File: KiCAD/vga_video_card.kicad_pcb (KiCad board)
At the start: 2 copper layers, 85 parts, among them J1 DE15_Socket_HighDensity, J2 Conn_01x20, J3 Conn_01x20, J4 Conn_01x20, J5 Conn_01x20, J6 Conn_02x16_Odd_Even, SW1 rst_btn, SW2 SW_DPDT_x2, SW3 SW_DPDT_x2, SW4 SW_DPDT_x2, U1 74HC161, U10 74HC04, U11 74HC112, U12 74HC32, U13 74HC173, U14 74HC173, U15 74HC161, U16 74HC161, U17 74HC161, U18 74HC04, U19 74HC04, U2 74HC161, U20 74HC133, U21 74HC133, U22 74HC133, U23 74HC133, U24 74HC112, U25 74HC173, U26 74HC173, U27 74HC04, U28 74HC253, U29 74HC253, U3 74HC161, U30 CY7C199, U31 CY7C199, U32 74AHC595, U33 74AHC595, U34 74AHC595, U35 AD7523JN, U36 LM358, U37 74HC257, U38 74HC257, U39 74HC02, U4 74HC04, U44 74HC257, U45 74HC257, U46 74HC257, U47 74HC257, U48 74HC257, U49 74HC257, U5 74HC04, U50 74HC257, U51 74HC257, U52 74HC4053, U53 74HC4053, U54 74HC4053, U55 74HC257, U56 74HC257, U6 74HC30, U7 74HC30, U8 74HC30, U9 74HC30, Y1 10MHz

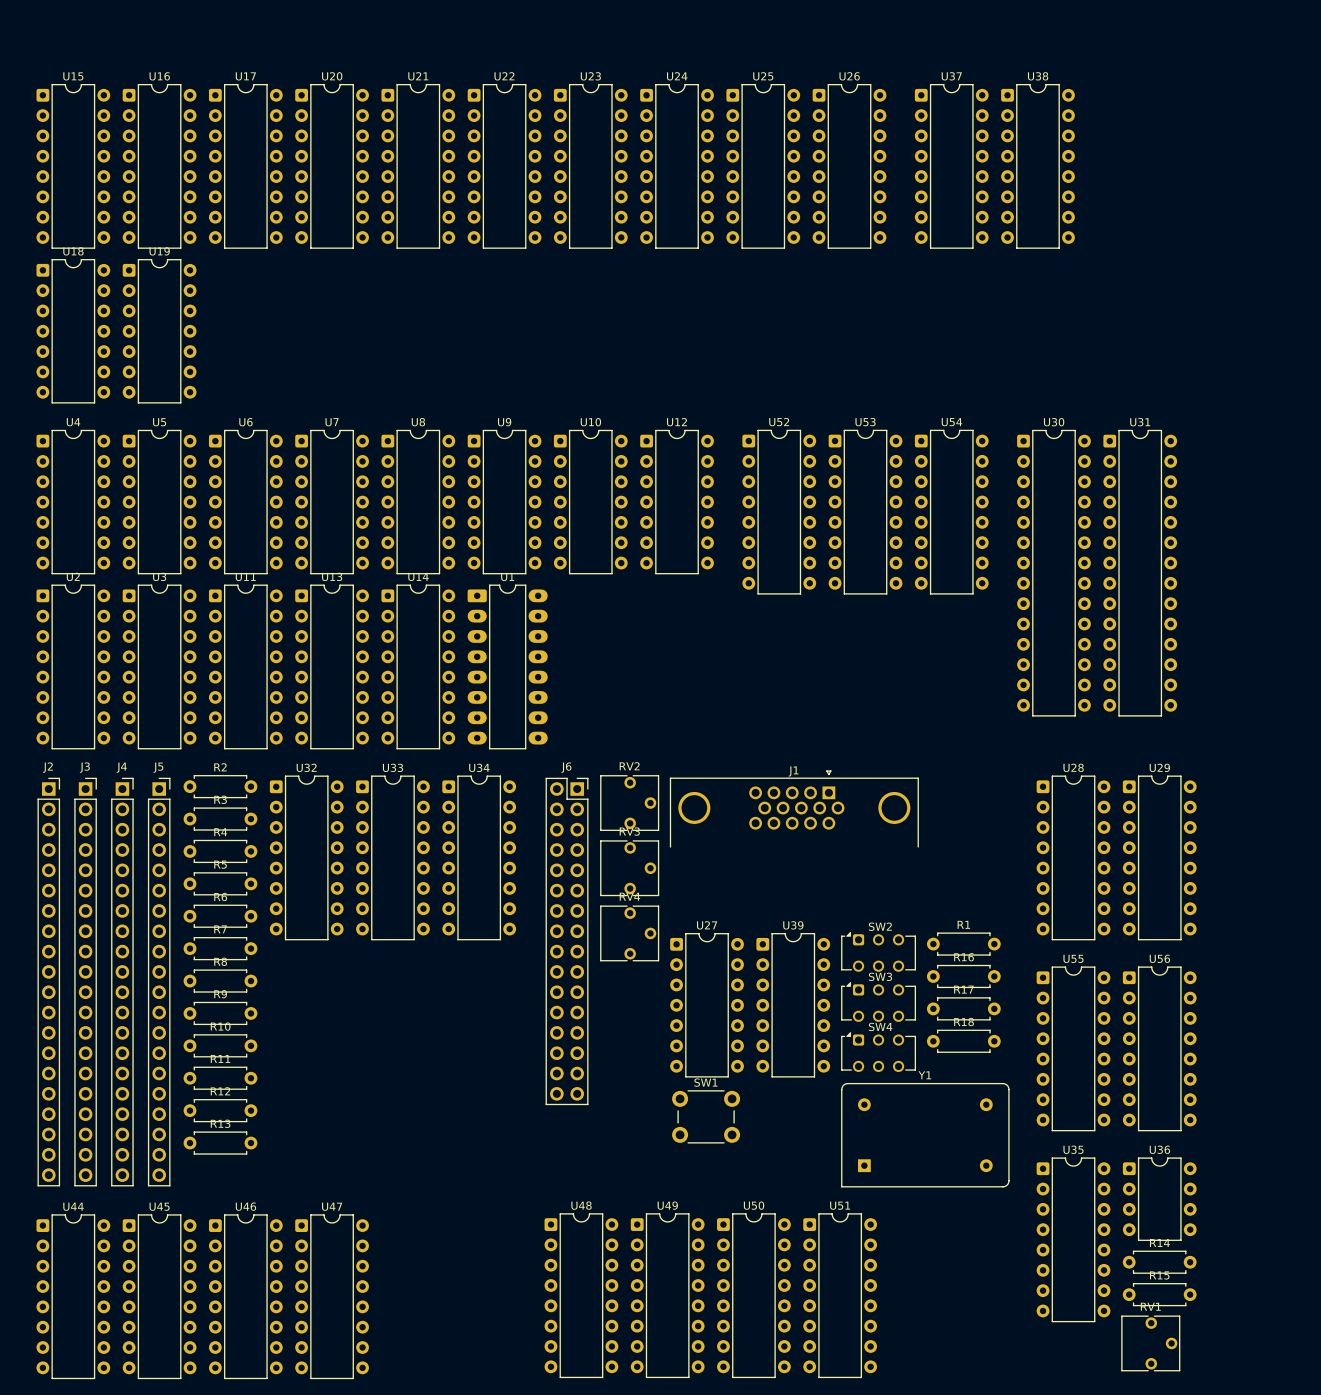
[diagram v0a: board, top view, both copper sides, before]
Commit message: modified debug connector; changed board type in pcb editor
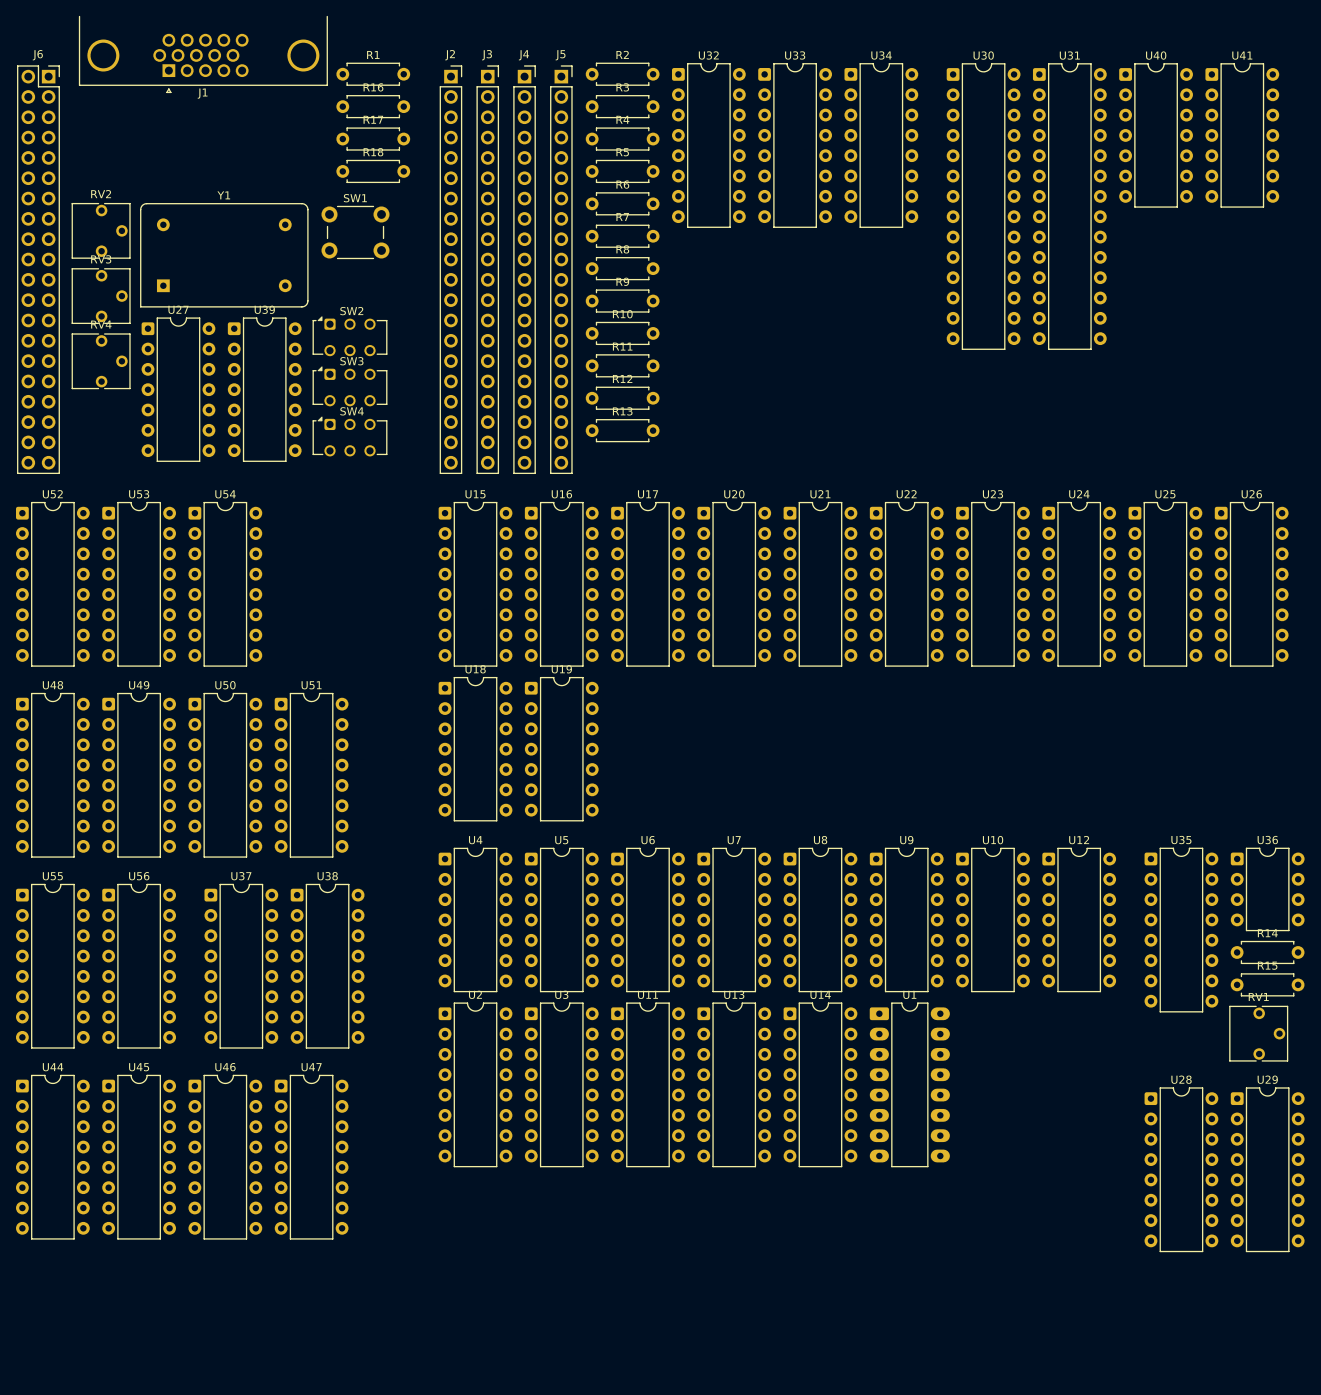
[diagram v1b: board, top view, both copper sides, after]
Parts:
- added U40: 74HC74, Package_DIP:DIP-14_W7.62mm, F.Cu at (164.4, 20.0)
- added U41: 74HC00, Package_DIP:DIP-14_W7.62mm, F.Cu at (175.2, 20.0)
- J6: value Conn_02x16_Odd_Even -> Conn_02x20_Odd_Even; footprint Connector_PinSocket_2.54mm:PinSocket_2x16_P2.54mm_Vertical -> Connector_PinSocket_2.54mm:PinSocket_2x20_P2.54mm_Vertical
- moved Y1 140.6 mm to (44.1, 46.4)
- moved U37 133.7 mm to (50.1, 122.6)
- moved U38 133.7 mm to (60.9, 122.6)
- moved R1 131.4 mm to (66.6, 19.9)
- moved R17 131.4 mm to (66.6, 28.1)
- moved R18 131.4 mm to (66.6, 32.1)
- moved R16 131.4 mm to (66.6, 24.0)
- moved U55 128.0 mm to (26.5, 122.6)
- moved U56 128.0 mm to (37.3, 122.6)
- moved J1 122.3 mm to (44.8, 19.5), turned to 180 degrees
- moved SW1 118.9 mm to (64.9, 37.5)
- moved J6 110.9 mm to (29.8, 20.2)
- moved R10 102.3 mm to (97.8, 52.4)
- moved R13 102.3 mm to (97.8, 64.5)
- moved R5 102.3 mm to (97.8, 32.1)
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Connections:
- net /RAM_module/RAM_state_controller/RAM0_~{WE} renamed /RAM0_~{WE}
- net /RAM_module/ext_graphics_source/data_rclk renamed /RAM_module/ext_graphics_rclk
- net Net-(J3-Pin_1) renamed /RAM_module/await_upd
- R1 pad 2: /horizontal_counter/manual_rst -> /mrst
- SW1 pad 1: /horizontal_counter/manual_rst -> /mrst
- U12 pad 13: /horizontal_counter/manual_rst -> /mrst
- U12 pad 5: /horizontal_counter/manual_rst -> /mrst
- U27 pad 3: unconnected-(U27-Pad3) -> (no net)
- U27 pad 4: unconnected-(U27-Pad4) -> (no net)
- U28 pad 7: /RAM_module/RAM_state_controller/RAM0_~{CE} -> /RAM0_~{CE}
- U29 pad 7: /RAM_module/RAM_state_controller/RAM1_~{CE} -> /RAM1_~{CE}
- U29 pad 9: /RAM_module/RAM_state_controller/RAM1_~{WE} -> /RAM1_~{WE}
- U30 pad 20: /RAM_module/RAM_state_controller/RAM0_~{CE} -> /RAM0_~{CE}
- U30 pad 22: /RAM_module/RAM_state_controller/RAM0_~{CE} -> /RAM0_~{CE}
- U31 pad 20: /RAM_module/RAM_state_controller/RAM1_~{CE} -> /RAM1_~{CE}
- U31 pad 22: /RAM_module/RAM_state_controller/RAM1_~{CE} -> /RAM1_~{CE}
- U31 pad 27: /RAM_module/RAM_state_controller/RAM1_~{WE} -> /RAM1_~{WE}
- U39 pad 4: unconnected-(U39-Pad4) -> /writing_RAM
- U39 pad 5: unconnected-(U39-Pad5) -> Net-(U39-Pad5)
- U39 pad 6: unconnected-(U39-Pad6) -> /mrst
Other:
- copper layers 2 -> 4

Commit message: update pcb
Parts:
- U1: footprint Package_DIP:DIP-16_W7.62mm_LongPads -> Package_DIP:DIP-16_W7.62mm
- moved U14 179.3 mm to (301.8, 134.4)
- moved J1 176.5 mm to (221.4, 18.2), turned to 0 degrees
- moved J2 168.5 mm to (248.6, 17.2)
- moved J3 168.5 mm to (253.2, 17.2)
- moved R10 168.5 mm to (266.2, 49.3)
- moved R11 168.5 mm to (266.2, 53.4)
- moved R12 168.5 mm to (266.2, 57.4)
- moved R13 168.5 mm to (266.2, 61.5)
- moved R14 168.5 mm to (346.9, 126.7)
- moved R15 168.5 mm to (346.9, 130.8)
- moved R16 168.5 mm to (235.1, 21.0)
- moved R17 168.5 mm to (235.1, 25.0)
- moved R18 168.5 mm to (235.1, 29.1)
- moved R2 168.5 mm to (266.2, 16.9)
- moved R3 168.5 mm to (266.2, 21.0)
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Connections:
- U27 pad 3: (no net) -> unconnected-(U27-Pad3)
- U27 pad 4: (no net) -> unconnected-(U27-Pad4)
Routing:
- net /horizontal_counter/CLK: track 0.00 -> 172.6 mm
- net /horizontal_counter/bit_2: track 0.00 -> 157.4 mm
- net /horizontal_counter/~{CLK}: track 0.00 -> 149.8 mm
- net /horizontal_counter/bit_0: track 0.00 -> 145.7 mm
- net /horizontal_counter/bit_3: track 0.00 -> 98.0 mm
- net /horizontal_counter/~{rst}: track 0.00 -> 67.9 mm
- net /horizontal_counter/bit_1: track 0.00 -> 60.6 mm
- net /horizontal_counter/~{bit_1}: track 0.00 -> 52.4 mm
- net /horizontal_counter/bit_7: track 0.00 -> 49.9 mm
- net /horizontal_counter/~{bit_2}: track 0.00 -> 39.9 mm
- net /horizontal_counter/bit_6: track 0.00 -> 38.9 mm
- net /horizontal_counter/bit_4: track 0.00 -> 36.0 mm
- net /horizontal_counter/bit_5: track 0.00 -> 35.1 mm
- net /horizontal_counter/~{bit_0}: track 0.00 -> 34.7 mm
- net /horizontal_counter/bit_8: track 0.00 -> 16.0 mm
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- added copper zone on In2.Cu, net +5V
- added copper zone on In1.Cu, net GND

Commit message: fix multiple ERCs that made RAM addrs not connecting
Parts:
- moved U25 285.9 mm to (48.3, 64.8)
- moved U26 282.7 mm to (62.2, 64.8)
- moved U14 270.8 mm to (34.3, 176.5)
- moved U24 261.6 mm to (62.2, 87.6)
- moved U22 256.1 mm to (48.3, 108.0)
- moved U23 253.3 mm to (62.2, 110.5)
- moved U20 239.3 mm to (48.3, 130.8)
- moved U21 236.9 mm to (62.2, 133.3)
- moved U17 235.8 mm to (48.3, 153.7)
- moved U31 228.3 mm to (116.8, 116.8)
- moved U15 225.4 mm to (48.3, 176.5)
- moved U16 222.6 mm to (62.2, 176.5)
- moved U19 210.5 mm to (48.3, 87.6)
- moved U13 205.5 mm to (20.3, 172.7)
- moved U30 199.8 mm to (111.8, 26.7)
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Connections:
- U52 pad 1: /RAM_module/RAM_bus_mux/RAM0_data1 -> /RAM_module/RAM0_d1
- U52 pad 12: /RAM_module/RAM_bus_mux/RAM1_data0 -> /RAM_module/RAM1_d0
- U52 pad 13: /RAM_module/RAM_bus_mux/RAM0_data0 -> /RAM_module/RAM0_d0
- U52 pad 2: /RAM_module/RAM_bus_mux/RAM1_data1 -> /RAM_module/RAM1_d1
- U52 pad 3: /RAM_module/RAM_bus_mux/RAM0_data2 -> /RAM_module/RAM0_d2
- U52 pad 5: /RAM_module/RAM_bus_mux/RAM1_data2 -> /RAM_module/RAM1_d2
- U53 pad 1: /RAM_module/RAM_bus_mux/RAM0_data4 -> /RAM_module/RAM0_d4
- U53 pad 12: /RAM_module/RAM_bus_mux/RAM1_data3 -> /RAM_module/RAM1_d3
- U53 pad 13: /RAM_module/RAM_bus_mux/RAM0_data3 -> /RAM_module/RAM0_d3
- U53 pad 2: /RAM_module/RAM_bus_mux/RAM1_data4 -> /RAM_module/RAM1_d4
- U53 pad 3: /RAM_module/RAM_bus_mux/RAM0_data5 -> /RAM_module/RAM0_d5
- U53 pad 5: /RAM_module/RAM_bus_mux/RAM1_data5 -> /RAM_module/RAM1_d5
- U54 pad 1: /RAM_module/RAM_bus_mux/RAM0_data7 -> /RAM_module/RAM0_d7
- U54 pad 12: /RAM_module/RAM_bus_mux/RAM1_data6 -> /RAM_module/RAM1_d6
- U54 pad 13: /RAM_module/RAM_bus_mux/RAM0_data6 -> /RAM_module/RAM0_d6
- U54 pad 2: /RAM_module/RAM_bus_mux/RAM1_data7 -> /RAM_module/RAM1_d7
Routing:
- net /horizontal_counter/CLK: track 172.6 -> 0.00 mm
- net /horizontal_counter/bit_2: track 157.4 -> 0.00 mm
- net /horizontal_counter/~{CLK}: track 149.8 -> 0.00 mm
- net /horizontal_counter/bit_0: track 145.7 -> 0.00 mm
- net /horizontal_counter/bit_3: track 98.0 -> 0.00 mm
- net /horizontal_counter/~{rst}: track 67.9 -> 0.00 mm
- net /horizontal_counter/bit_1: track 60.6 -> 0.00 mm
- net /horizontal_counter/~{bit_1}: track 52.4 -> 0.00 mm
- net /horizontal_counter/bit_7: track 49.9 -> 0.00 mm
- net /horizontal_counter/~{bit_2}: track 39.9 -> 0.00 mm
- net /horizontal_counter/bit_6: track 38.9 -> 0.00 mm
- net /horizontal_counter/bit_4: track 36.0 -> 0.00 mm
- net /horizontal_counter/bit_5: track 35.1 -> 0.00 mm
- net /horizontal_counter/~{bit_0}: track 34.7 -> 0.00 mm
- net /horizontal_counter/bit_8: track 16.0 -> 0.00 mm
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- removed copper zone on In2.Cu, net +5V
- removed copper zone on In1.Cu, net GND

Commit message: resolved all ERC errors, kicad got some stupid bugs
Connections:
- net /i_addr0 renamed /RAM_module/RAM_bus_mux/i_addr0
- net /i_addr1 renamed /RAM_module/RAM_bus_mux/i_addr1
- net /i_addr2 renamed /RAM_module/RAM_bus_mux/i_addr2
- net /i_addr3 renamed /RAM_module/RAM_bus_mux/i_addr3
- net /i_addr4 renamed /RAM_module/RAM_bus_mux/i_addr4
- net /i_addr5 renamed /RAM_module/RAM_bus_mux/i_addr5
- net /i_addr6 renamed /RAM_module/RAM_bus_mux/i_addr6
- net /i_addr7 renamed /RAM_module/RAM_bus_mux/i_addr7
- J6 pad 10: /j_addr_3 -> /RAM_module/RAM_bus_mux/j_addr3
- J6 pad 12: /j_addr_4 -> /RAM_module/RAM_bus_mux/j_addr4
- J6 pad 14: /j_addr_5 -> /RAM_module/RAM_bus_mux/j_addr5
- J6 pad 16: /j_addr_6 -> /RAM_module/RAM_bus_mux/j_addr6
- J6 pad 18: /j_addr_7 -> /RAM_module/RAM_bus_mux/j_addr7
- J6 pad 35: unconnected-(J6-Pin_35-Pad35) -> /RAM0_~{WE}
- J6 pad 4: /j_addr_0 -> /RAM_module/RAM_bus_mux/j_addr0
- J6 pad 6: /j_addr_1 -> /RAM_module/RAM_bus_mux/j_addr1
- J6 pad 8: /j_addr_2 -> /RAM_module/RAM_bus_mux/j_addr2
- U13 pad 3: /j_addr0 -> /RAM_module/RAM_bus_mux/j_addr0
- U13 pad 4: /j_addr1 -> /RAM_module/RAM_bus_mux/j_addr1
- U13 pad 5: /j_addr2 -> /RAM_module/RAM_bus_mux/j_addr2
- U13 pad 6: /j_addr3 -> /RAM_module/RAM_bus_mux/j_addr3
- U14 pad 3: /j_addr4 -> /RAM_module/RAM_bus_mux/j_addr4
- U14 pad 4: /j_addr5 -> /RAM_module/RAM_bus_mux/j_addr5
- U14 pad 5: /j_addr6 -> /RAM_module/RAM_bus_mux/j_addr6
- U14 pad 6: /j_addr7 -> /RAM_module/RAM_bus_mux/j_addr7
- U15 pad 1: unconnected-(U15-~{MR}-Pad1) -> /vertical_counter/~{rst}
- U16 pad 1: unconnected-(U16-~{MR}-Pad1) -> /vertical_counter/~{rst}
- U17 pad 1: unconnected-(U17-~{MR}-Pad1) -> /vertical_counter/~{rst}
- U25 pad 16: unconnected-(U25-VCC-Pad16) -> +5V
- U28 pad 14: /RAM_module/RAM_bus_mux/rbit_0 -> /RAM_module/RAM_bus_mux/j_addr0
- U29 pad 14: /RAM_module/RAM_bus_mux/rbit_0 -> /RAM_module/RAM_bus_mux/j_addr0
- U32 pad 1: /RAM_module/RAM_bus_mux/15bit_2:1_MUX/I1_8 -> /RAM_module/RAM_bus_mux/w_addr8
- U32 pad 2: /RAM_module/RAM_bus_mux/15bit_2:1_MUX/I1_9 -> /RAM_module/RAM_bus_mux/w_addr9
- U32 pad 3: /RAM_module/RAM_bus_mux/15bit_2:1_MUX/I1_10 -> /RAM_module/RAM_bus_mux/w_addr10
- U32 pad 4: /RAM_module/RAM_bus_mux/15bit_2:1_MUX/I1_11 -> /RAM_module/RAM_bus_mux/w_addr11
- U32 pad 5: /RAM_module/RAM_bus_mux/15bit_2:1_MUX/I1_12 -> /RAM_module/RAM_bus_mux/w_addr12
- U32 pad 6: /RAM_module/RAM_bus_mux/15bit_2:1_MUX/I1_13 -> /RAM_module/RAM_bus_mux/w_addr13
- U32 pad 7: /RAM_module/RAM_bus_mux/15bit_2:1_MUX/I1_14 -> /RAM_module/RAM_bus_mux/w_addr14
- U33 pad 1: /RAM_module/RAM_bus_mux/15bit_2:1_MUX/I1_1 -> /RAM_module/RAM_bus_mux/w_addr1
- U33 pad 15: /RAM_module/RAM_bus_mux/15bit_2:1_MUX/I1_0 -> /RAM_module/RAM_bus_mux/w_addr0
- U33 pad 2: /RAM_module/RAM_bus_mux/15bit_2:1_MUX/I1_2 -> /RAM_module/RAM_bus_mux/w_addr2
- U33 pad 3: /RAM_module/RAM_bus_mux/15bit_2:1_MUX/I1_3 -> /RAM_module/RAM_bus_mux/w_addr3
- U33 pad 4: /RAM_module/RAM_bus_mux/15bit_2:1_MUX/I1_4 -> /RAM_module/RAM_bus_mux/w_addr4
- U33 pad 5: /RAM_module/RAM_bus_mux/15bit_2:1_MUX/I1_5 -> /RAM_module/RAM_bus_mux/w_addr5
- U33 pad 6: /RAM_module/RAM_bus_mux/15bit_2:1_MUX/I1_6 -> /RAM_module/RAM_bus_mux/w_addr6
- U33 pad 7: /RAM_module/RAM_bus_mux/15bit_2:1_MUX/I1_7 -> /RAM_module/RAM_bus_mux/w_addr7
- U37 pad 10: unconnected-(U37-I1d-Pad10) -> /ADC_module/I3
- U37 pad 11: unconnected-(U37-I0d-Pad11) -> GND
- U37 pad 12: unconnected-(U37-Zc-Pad12) -> /ADC_module/D2
- U37 pad 13: unconnected-(U37-I1c-Pad13) -> /ADC_module/I2
- U37 pad 14: unconnected-(U37-I0c-Pad14) -> GND
- U37 pad 2: unconnected-(U37-I0a-Pad2) -> GND
- U37 pad 3: unconnected-(U37-I1a-Pad3) -> /ADC_module/I0
- U37 pad 4: unconnected-(U37-Za-Pad4) -> /ADC_module/D0
- U37 pad 5: unconnected-(U37-I0b-Pad5) -> GND
- U37 pad 6: unconnected-(U37-I1b-Pad6) -> /ADC_module/I1
- U37 pad 7: unconnected-(U37-Zb-Pad7) -> /ADC_module/D1
- U37 pad 9: unconnected-(U37-Zd-Pad9) -> /ADC_module/D3
- U38 pad 10: unconnected-(U38-I1d-Pad10) -> /ADC_module/I7
- U38 pad 11: unconnected-(U38-I0d-Pad11) -> GND
- U38 pad 12: unconnected-(U38-Zc-Pad12) -> /ADC_module/D6
- U38 pad 13: unconnected-(U38-I1c-Pad13) -> /ADC_module/I6
- U38 pad 14: unconnected-(U38-I0c-Pad14) -> GND
- U38 pad 2: unconnected-(U38-I0a-Pad2) -> GND
- U38 pad 3: unconnected-(U38-I1a-Pad3) -> /ADC_module/I4
- U38 pad 4: unconnected-(U38-Za-Pad4) -> /ADC_module/D4
- U38 pad 5: unconnected-(U38-I0b-Pad5) -> GND
- U38 pad 6: unconnected-(U38-I1b-Pad6) -> /ADC_module/I5
- U38 pad 7: unconnected-(U38-Zb-Pad7) -> /ADC_module/D5
- U38 pad 9: unconnected-(U38-Zd-Pad9) -> /ADC_module/D7
- U40 pad 4: unconnected-(U40A-~{S}-Pad4) -> +5V
- U44 pad 1: /RAM_module/RAM_bus_mux/rbit_0 -> /RAM_module/RAM_bus_mux/j_addr0
- U44 pad 10: unconnected-(U44-I1d-Pad10) -> /RAM_module/RAM_bus_mux/w_addr3
- U44 pad 11: unconnected-(U44-I0d-Pad11) -> /RAM_module/RAM_bus_mux/addr3
- U44 pad 12: unconnected-(U44-Zc-Pad12) -> /RAM_module/RAM0_a2
- U44 pad 13: unconnected-(U44-I1c-Pad13) -> /RAM_module/RAM_bus_mux/w_addr2
- U44 pad 14: unconnected-(U44-I0c-Pad14) -> /RAM_module/RAM_bus_mux/addr2
- U44 pad 2: unconnected-(U44-I0a-Pad2) -> /RAM_module/RAM_bus_mux/addr0
- U44 pad 3: unconnected-(U44-I1a-Pad3) -> /RAM_module/RAM_bus_mux/w_addr0
- U44 pad 4: unconnected-(U44-Za-Pad4) -> /RAM_module/RAM0_a0
- U44 pad 5: unconnected-(U44-I0b-Pad5) -> /RAM_module/RAM_bus_mux/addr1
- U44 pad 6: unconnected-(U44-I1b-Pad6) -> /RAM_module/RAM_bus_mux/w_addr1
- U44 pad 7: unconnected-(U44-Zb-Pad7) -> /RAM_module/RAM0_a1
- U44 pad 9: unconnected-(U44-Zd-Pad9) -> /RAM_module/RAM0_a3
- U45 pad 1: /RAM_module/RAM_bus_mux/rbit_0 -> /RAM_module/RAM_bus_mux/j_addr0
- U45 pad 10: unconnected-(U45-I1d-Pad10) -> /RAM_module/RAM_bus_mux/w_addr7
- U45 pad 11: unconnected-(U45-I0d-Pad11) -> /RAM_module/RAM_bus_mux/addr7
- U45 pad 12: unconnected-(U45-Zc-Pad12) -> /RAM_module/RAM0_a6
- U45 pad 13: unconnected-(U45-I1c-Pad13) -> /RAM_module/RAM_bus_mux/w_addr6
- U45 pad 14: unconnected-(U45-I0c-Pad14) -> /RAM_module/RAM_bus_mux/addr6
- U45 pad 2: unconnected-(U45-I0a-Pad2) -> /RAM_module/RAM_bus_mux/addr4
- U45 pad 3: unconnected-(U45-I1a-Pad3) -> /RAM_module/RAM_bus_mux/w_addr4
- U45 pad 4: unconnected-(U45-Za-Pad4) -> /RAM_module/RAM0_a4
- U45 pad 5: unconnected-(U45-I0b-Pad5) -> /RAM_module/RAM_bus_mux/addr5
- U45 pad 6: unconnected-(U45-I1b-Pad6) -> /RAM_module/RAM_bus_mux/w_addr5
- U45 pad 7: unconnected-(U45-Zb-Pad7) -> /RAM_module/RAM0_a5
- U45 pad 9: unconnected-(U45-Zd-Pad9) -> /RAM_module/RAM0_a7
- U46 pad 1: /RAM_module/RAM_bus_mux/rbit_0 -> /RAM_module/RAM_bus_mux/j_addr0
- U46 pad 10: unconnected-(U46-I1d-Pad10) -> /RAM_module/RAM_bus_mux/w_addr11
- U46 pad 11: unconnected-(U46-I0d-Pad11) -> /RAM_module/RAM_bus_mux/addr11
- U46 pad 12: unconnected-(U46-Zc-Pad12) -> /RAM_module/RAM0_a10
- U46 pad 13: unconnected-(U46-I1c-Pad13) -> /RAM_module/RAM_bus_mux/w_addr10
- U46 pad 14: unconnected-(U46-I0c-Pad14) -> /RAM_module/RAM_bus_mux/addr10
- U46 pad 2: unconnected-(U46-I0a-Pad2) -> /RAM_module/RAM_bus_mux/addr8
- U46 pad 3: unconnected-(U46-I1a-Pad3) -> /RAM_module/RAM_bus_mux/w_addr8
- U46 pad 4: unconnected-(U46-Za-Pad4) -> /RAM_module/RAM0_a8
- U46 pad 5: unconnected-(U46-I0b-Pad5) -> /RAM_module/RAM_bus_mux/addr9
- U46 pad 6: unconnected-(U46-I1b-Pad6) -> /RAM_module/RAM_bus_mux/w_addr9
- U46 pad 7: unconnected-(U46-Zb-Pad7) -> /RAM_module/RAM0_a9
- U46 pad 9: unconnected-(U46-Zd-Pad9) -> /RAM_module/RAM0_a11
- U47 pad 1: /RAM_module/RAM_bus_mux/rbit_0 -> /RAM_module/RAM_bus_mux/j_addr0
- U47 pad 12: unconnected-(U47-Zc-Pad12) -> /RAM_module/RAM0_a14
- U47 pad 13: unconnected-(U47-I1c-Pad13) -> /RAM_module/RAM_bus_mux/w_addr14
- U47 pad 14: unconnected-(U47-I0c-Pad14) -> /RAM_module/RAM_bus_mux/addr14
- U47 pad 2: unconnected-(U47-I0a-Pad2) -> /RAM_module/RAM_bus_mux/addr12
- U47 pad 3: unconnected-(U47-I1a-Pad3) -> /RAM_module/RAM_bus_mux/w_addr12
- U47 pad 4: unconnected-(U47-Za-Pad4) -> /RAM_module/RAM0_a12
- U47 pad 5: unconnected-(U47-I0b-Pad5) -> /RAM_module/RAM_bus_mux/addr13
- U47 pad 6: unconnected-(U47-I1b-Pad6) -> /RAM_module/RAM_bus_mux/w_addr13
- U47 pad 7: unconnected-(U47-Zb-Pad7) -> /RAM_module/RAM0_a13
- U48 pad 1: /RAM_module/RAM_bus_mux/rbit_0 -> /RAM_module/RAM_bus_mux/j_addr0
- U48 pad 10: unconnected-(U48-I1d-Pad10) -> /RAM_module/RAM_bus_mux/addr3
- U48 pad 11: unconnected-(U48-I0d-Pad11) -> /RAM_module/RAM_bus_mux/w_addr3
- U48 pad 12: unconnected-(U48-Zc-Pad12) -> /RAM_module/RAM1_a2
- U48 pad 13: unconnected-(U48-I1c-Pad13) -> /RAM_module/RAM_bus_mux/addr2
- U48 pad 14: unconnected-(U48-I0c-Pad14) -> /RAM_module/RAM_bus_mux/w_addr2
- U48 pad 2: unconnected-(U48-I0a-Pad2) -> /RAM_module/RAM_bus_mux/w_addr0
- U48 pad 3: unconnected-(U48-I1a-Pad3) -> /RAM_module/RAM_bus_mux/addr0
- U48 pad 4: unconnected-(U48-Za-Pad4) -> /RAM_module/RAM1_a0
- U48 pad 5: unconnected-(U48-I0b-Pad5) -> /RAM_module/RAM_bus_mux/w_addr1
- U48 pad 6: unconnected-(U48-I1b-Pad6) -> /RAM_module/RAM_bus_mux/addr1
- U48 pad 7: unconnected-(U48-Zb-Pad7) -> /RAM_module/RAM1_a1
- U48 pad 9: unconnected-(U48-Zd-Pad9) -> /RAM_module/RAM1_a3
- U49 pad 1: /RAM_module/RAM_bus_mux/rbit_0 -> /RAM_module/RAM_bus_mux/j_addr0
- U49 pad 10: unconnected-(U49-I1d-Pad10) -> /RAM_module/RAM_bus_mux/addr7
- U49 pad 11: unconnected-(U49-I0d-Pad11) -> /RAM_module/RAM_bus_mux/w_addr7
- U49 pad 12: unconnected-(U49-Zc-Pad12) -> /RAM_module/RAM1_a6
- U49 pad 13: unconnected-(U49-I1c-Pad13) -> /RAM_module/RAM_bus_mux/addr6
- U49 pad 14: unconnected-(U49-I0c-Pad14) -> /RAM_module/RAM_bus_mux/w_addr6
- U49 pad 2: unconnected-(U49-I0a-Pad2) -> /RAM_module/RAM_bus_mux/w_addr4
- U49 pad 3: unconnected-(U49-I1a-Pad3) -> /RAM_module/RAM_bus_mux/addr4
- U49 pad 4: unconnected-(U49-Za-Pad4) -> /RAM_module/RAM1_a4
- U49 pad 5: unconnected-(U49-I0b-Pad5) -> /RAM_module/RAM_bus_mux/w_addr5
- U49 pad 6: unconnected-(U49-I1b-Pad6) -> /RAM_module/RAM_bus_mux/addr5
- U49 pad 7: unconnected-(U49-Zb-Pad7) -> /RAM_module/RAM1_a5
- U49 pad 9: unconnected-(U49-Zd-Pad9) -> /RAM_module/RAM1_a7
- U50 pad 1: /RAM_module/RAM_bus_mux/rbit_0 -> /RAM_module/RAM_bus_mux/j_addr0
- U50 pad 10: unconnected-(U50-I1d-Pad10) -> /RAM_module/RAM_bus_mux/addr11
- U50 pad 11: unconnected-(U50-I0d-Pad11) -> /RAM_module/RAM_bus_mux/w_addr11
- U50 pad 12: unconnected-(U50-Zc-Pad12) -> /RAM_module/RAM1_a10
- U50 pad 13: unconnected-(U50-I1c-Pad13) -> /RAM_module/RAM_bus_mux/addr10
- U50 pad 14: unconnected-(U50-I0c-Pad14) -> /RAM_module/RAM_bus_mux/w_addr10
- U50 pad 2: unconnected-(U50-I0a-Pad2) -> /RAM_module/RAM_bus_mux/w_addr8
- U50 pad 3: unconnected-(U50-I1a-Pad3) -> /RAM_module/RAM_bus_mux/addr8
- U50 pad 4: unconnected-(U50-Za-Pad4) -> /RAM_module/RAM1_a8
- U50 pad 5: unconnected-(U50-I0b-Pad5) -> /RAM_module/RAM_bus_mux/w_addr9
- U50 pad 6: unconnected-(U50-I1b-Pad6) -> /RAM_module/RAM_bus_mux/addr9
- U50 pad 7: unconnected-(U50-Zb-Pad7) -> /RAM_module/RAM1_a9
- U50 pad 9: unconnected-(U50-Zd-Pad9) -> /RAM_module/RAM1_a11
- U51 pad 1: /RAM_module/RAM_bus_mux/rbit_0 -> /RAM_module/RAM_bus_mux/j_addr0
- U51 pad 12: unconnected-(U51-Zc-Pad12) -> /RAM_module/RAM1_a14
- U51 pad 13: unconnected-(U51-I1c-Pad13) -> /RAM_module/RAM_bus_mux/addr14
- U51 pad 14: unconnected-(U51-I0c-Pad14) -> /RAM_module/RAM_bus_mux/w_addr14
- U51 pad 2: unconnected-(U51-I0a-Pad2) -> /RAM_module/RAM_bus_mux/w_addr12
- U51 pad 3: unconnected-(U51-I1a-Pad3) -> /RAM_module/RAM_bus_mux/addr12
- U51 pad 4: unconnected-(U51-Za-Pad4) -> /RAM_module/RAM1_a12
- U51 pad 5: unconnected-(U51-I0b-Pad5) -> /RAM_module/RAM_bus_mux/w_addr13
- U51 pad 6: unconnected-(U51-I1b-Pad6) -> /RAM_module/RAM_bus_mux/addr13
- U51 pad 7: unconnected-(U51-Zb-Pad7) -> /RAM_module/RAM1_a13
- U52 pad 10: /RAM_module/RAM_bus_mux/rbit_0 -> /RAM_module/RAM_bus_mux/j_addr0
- U52 pad 11: /RAM_module/RAM_bus_mux/rbit_0 -> /RAM_module/RAM_bus_mux/j_addr0
- U52 pad 9: /RAM_module/RAM_bus_mux/rbit_0 -> /RAM_module/RAM_bus_mux/j_addr0
- U53 pad 10: /RAM_module/RAM_bus_mux/rbit_0 -> /RAM_module/RAM_bus_mux/j_addr0
- U53 pad 11: /RAM_module/RAM_bus_mux/rbit_0 -> /RAM_module/RAM_bus_mux/j_addr0
- U53 pad 9: /RAM_module/RAM_bus_mux/rbit_0 -> /RAM_module/RAM_bus_mux/j_addr0
- U54 pad 10: /RAM_module/RAM_bus_mux/rbit_0 -> /RAM_module/RAM_bus_mux/j_addr0
- U54 pad 11: /RAM_module/RAM_bus_mux/rbit_0 -> /RAM_module/RAM_bus_mux/j_addr0
- U54 pad 9: /RAM_module/RAM_bus_mux/rbit_0 -> /RAM_module/RAM_bus_mux/j_addr0
- U55 pad 1: /RAM_module/RAM_bus_mux/rbit_0 -> /RAM_module/RAM_bus_mux/j_addr0
- U55 pad 10: unconnected-(U55-I1d-Pad10) -> /RAM_module/RAM1_d3
- U55 pad 11: unconnected-(U55-I0d-Pad11) -> /RAM_module/RAM0_d3
- U55 pad 12: unconnected-(U55-Zc-Pad12) -> /ADC_module/I2
- U55 pad 13: unconnected-(U55-I1c-Pad13) -> /RAM_module/RAM1_d2
- U55 pad 14: unconnected-(U55-I0c-Pad14) -> /RAM_module/RAM0_d2
- U55 pad 2: unconnected-(U55-I0a-Pad2) -> /RAM_module/RAM0_d0
- U55 pad 3: unconnected-(U55-I1a-Pad3) -> /RAM_module/RAM1_d0
- U55 pad 4: unconnected-(U55-Za-Pad4) -> /ADC_module/I0
- U55 pad 5: unconnected-(U55-I0b-Pad5) -> /RAM_module/RAM0_d1
- U55 pad 6: unconnected-(U55-I1b-Pad6) -> /RAM_module/RAM1_d1
- U55 pad 7: unconnected-(U55-Zb-Pad7) -> /ADC_module/I1
- U55 pad 9: unconnected-(U55-Zd-Pad9) -> /ADC_module/I3
- U56 pad 1: /RAM_module/RAM_bus_mux/rbit_0 -> /RAM_module/RAM_bus_mux/j_addr0
- U56 pad 10: unconnected-(U56-I1d-Pad10) -> /RAM_module/RAM1_d7
- U56 pad 11: unconnected-(U56-I0d-Pad11) -> /RAM_module/RAM0_d7
- U56 pad 12: unconnected-(U56-Zc-Pad12) -> /ADC_module/I6
- U56 pad 13: unconnected-(U56-I1c-Pad13) -> /RAM_module/RAM1_d6
- U56 pad 14: unconnected-(U56-I0c-Pad14) -> /RAM_module/RAM0_d6
- U56 pad 2: unconnected-(U56-I0a-Pad2) -> /RAM_module/RAM0_d4
- U56 pad 3: unconnected-(U56-I1a-Pad3) -> /RAM_module/RAM1_d4
- U56 pad 4: unconnected-(U56-Za-Pad4) -> /ADC_module/I4
- U56 pad 5: unconnected-(U56-I0b-Pad5) -> /RAM_module/RAM0_d5
- U56 pad 6: unconnected-(U56-I1b-Pad6) -> /RAM_module/RAM1_d5
- U56 pad 7: unconnected-(U56-Zb-Pad7) -> /ADC_module/I5
- U56 pad 9: unconnected-(U56-Zd-Pad9) -> /ADC_module/I7
